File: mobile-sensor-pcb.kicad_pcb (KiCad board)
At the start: 2 copper layers, 101.6 x 53.3 mm, 93 parts, among them J1 SMA, J2 USB_OTG, J3 JST PH, Q1 PNP-BJT-BIASED_SOT, SW1 RESET, SW2 ON/OFF, U1 3M_2908-05WB-MG, U10 LP2980AIM5-3.3/NOPB, U11 LP2980AIM5-3.3/NOPB, U12 LP2980AIM5-3.3/NOPB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

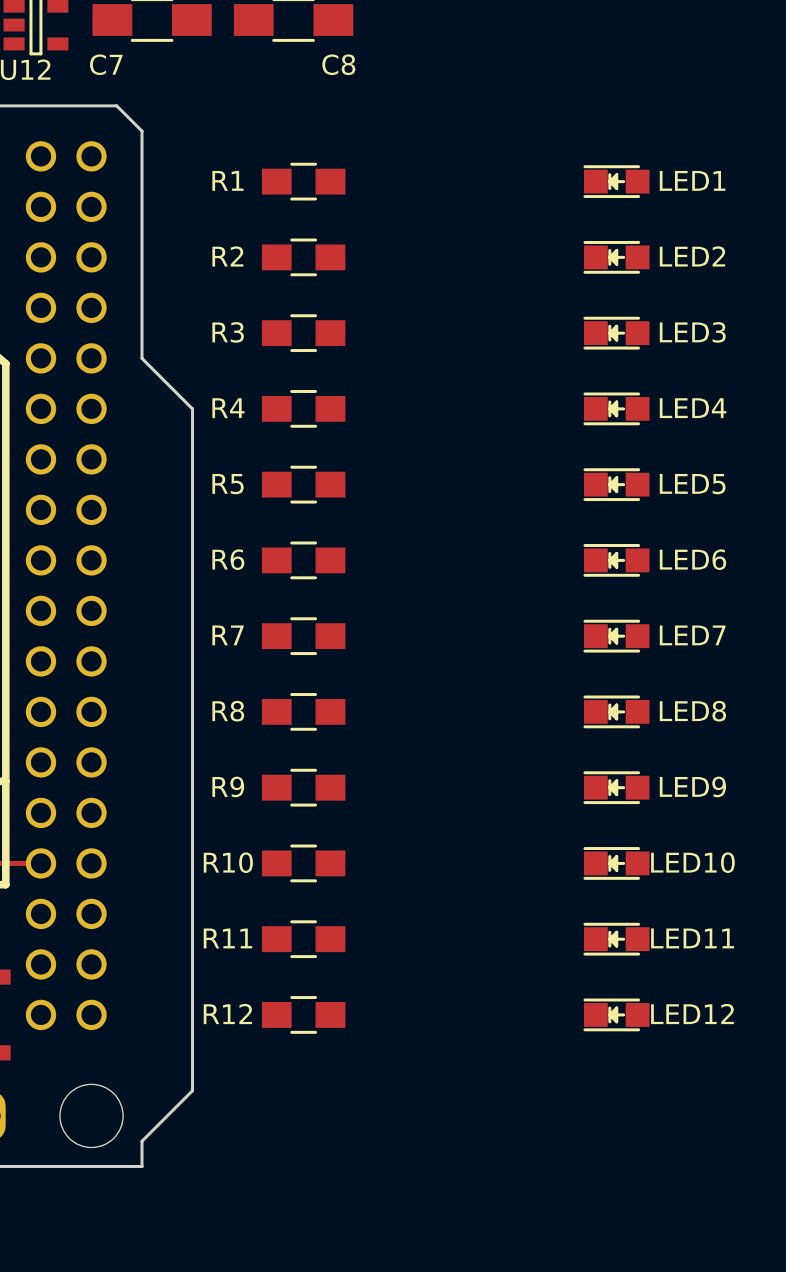
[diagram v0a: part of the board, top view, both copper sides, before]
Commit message: Tweak LED layout a little
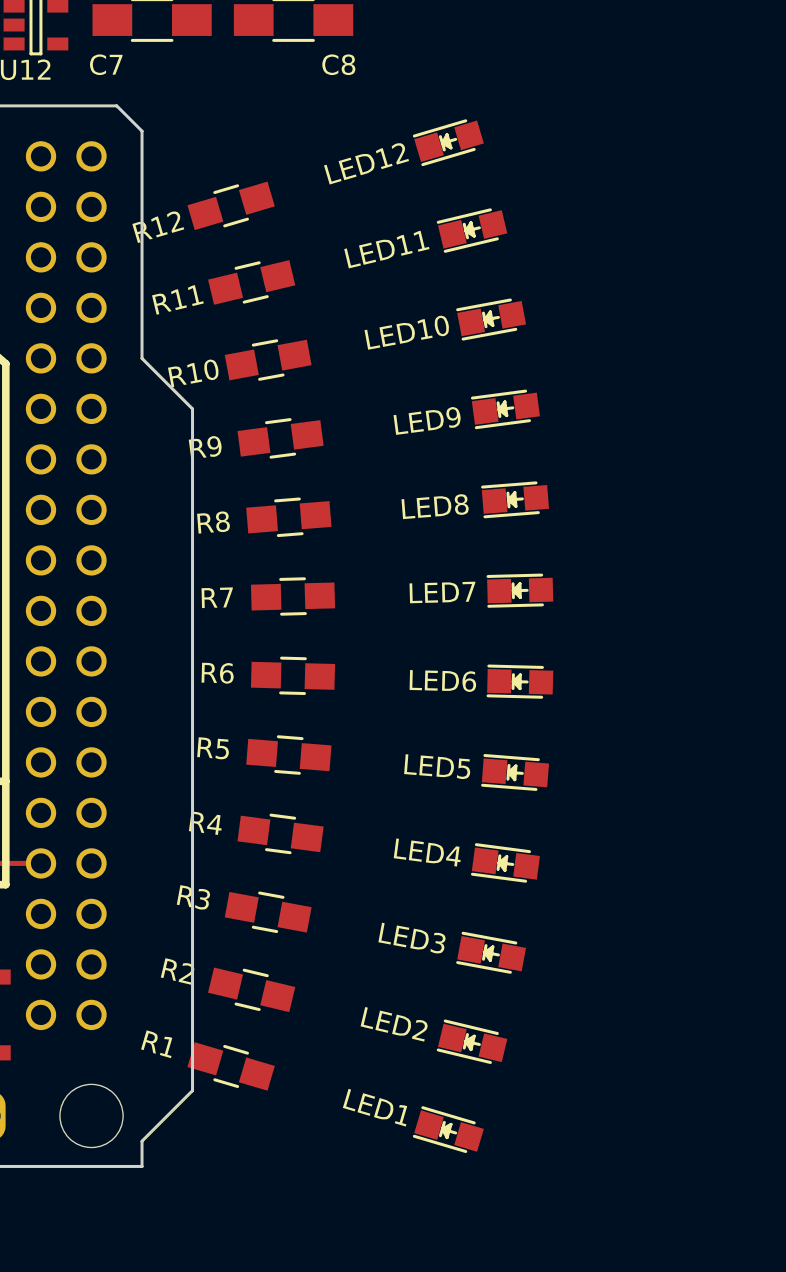
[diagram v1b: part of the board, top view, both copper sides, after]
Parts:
- moved LED1 48.5 mm to (165.3, 150.6), turned to 343.5 degrees
- moved LED12 44.7 mm to (165.3, 100.8), turned to 16.5 degrees
- moved R1 44.7 mm to (154.3, 147.4), turned to 343.5 degrees
- moved R12 40.9 mm to (154.3, 104.1), turned to 16.5 degrees
- moved LED2 40.2 mm to (166.5, 146.2), turned to 346.5 degrees
- moved R2 36.9 mm to (155.4, 143.5), turned to 346.5 degrees
- moved LED11 36.4 mm to (166.5, 105.3), turned to 13.5 degrees
- moved R11 33.1 mm to (155.4, 107.9), turned to 13.5 degrees
- moved LED3 31.8 mm to (167.4, 141.7), turned to 349.5 degrees
- moved R3 29.2 mm to (156.2, 139.6), turned to 349.5 degrees
- moved LED10 28.1 mm to (167.4, 109.8), turned to 10.5 degrees
- moved R10 25.4 mm to (156.2, 111.8), turned to 10.5 degrees
- moved LED4 23.5 mm to (168.2, 137.2), turned to 352.5 degrees
- moved R4 21.4 mm to (156.8, 135.7), turned to 352.5 degrees
- moved LED9 19.9 mm to (168.2, 114.3), turned to 7.5 degrees
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
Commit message: More routing
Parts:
- moved Q1 16.1 mm to (119.8, 106.2)
- moved C21 12.9 mm to (103.8, 115.1), turned to 270 degrees
- moved D1 6.84 mm to (112.9, 106.2), turned to 270 degrees
- moved F1 5.88 mm to (111.6, 112.5), turned to 270 degrees
- moved C20 5.59 mm to (106.4, 115.1), turned to 270 degrees
- turned R1 to 163.5 degrees
- turned R10 to 190.5 degrees
- turned R11 to 193.5 degrees
- turned R12 to 196.5 degrees
- turned R2 to 166.5 degrees
- turned R3 to 169.5 degrees
- turned R4 to 172.5 degrees
- turned R5 to 175.5 degrees
- turned R6 to 178.5 degrees
- turned R7 to 181.5 degrees
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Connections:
- C1 pad 1: Net-(C1-Pad1) -> BATT-5V
- C2 pad 1: Net-(C2-Pad1) -> XBEE-3V3
- R23 pad 1: Net-(R23-Pad1) -> Net-(C20-Pad1)
- R24 pad 1: Net-(R24-Pad1) -> Net-(C11-Pad1)
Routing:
- net GND: track 295.3 -> 460.8 mm, vias 6 -> 13
- net BATT-5V: track 9.49 -> 87.9 mm, vias 2 -> 5
- net SD-SCK: track 0.00 -> 77.1 mm, vias 0 -> 2
- net SD-MOSI: track 0.00 -> 71.7 mm, vias 0 -> 3
- net SD-CS: track 5.92 -> 77.0 mm, vias 0 -> 2
- net XBEE-RESET: track 0.00 -> 67.2 mm, vias 0 -> 2
- net XBEE-3V3: track 0.00 -> 67.0 mm, vias 0 -> 5
- net XBEE-RX: track 0.00 -> 51.3 mm, vias 0 -> 1
- net XBEE-TX: track 0.00 -> 50.9 mm, vias 0 -> 2
- net Net-(C20-Pad1): track 9.14 -> 52.3 mm, vias 0 -> 2
- net XBEE-DIO5: track 0.00 -> 32.9 mm, vias 0 -> 1
- net TC-SCK: track 0.00 -> 28.8 mm
- net Net-(C15-Pad2): track 0.00 -> 25.7 mm, vias 0 -> 1
- net TC-MISO: track 0.00 -> 24.9 mm
- net Net-(BT1-Pad1): track 0.00 -> 23.1 mm, vias 0 -> 1
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
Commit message: Route all but thermocouples. Add LED arc screenshots.
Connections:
- SHIELD1 pad 50: SD-SCK -> SD-CLK
- U2 pad 3: SD-SCK -> SD-CLK
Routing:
- net BATT-STAT: track 1.69 -> 137.2 mm, vias 1 -> 5
- net SD-CLK: track 1.59 -> 131.3 mm, vias 1 -> 4
- net GPS-FIX: track 1.63 -> 126.6 mm, vias 1 -> 4
- net USB-5V: track 13.5 -> 137.9 mm, vias 1 -> 4
- net GND: track 460.8 -> 558.5 mm
- net GPS-SD-3V3: track 75.7 -> 169.3 mm, vias 3 -> 6
- net BATT-5V: track 87.9 -> 172.6 mm, vias 5 -> 9
- net SD-SCK: track 77.1 -> 0.00 mm, vias 2 -> 0
- net XBEE-RSSI: track 1.59 -> 69.4 mm
- net GPS-TX: track 0.00 -> 61.9 mm, vias 0 -> 2
- net BATT-DEAD: track 1.56 -> 57.4 mm, vias 1 -> 2
- net TC-CS2: track 0.00 -> 47.9 mm, vias 0 -> 1
- net XBEE-3V3: track 67.0 -> 113.0 mm, vias 5 -> 6
- net GPS-5V-RX: track 20.3 -> 55.0 mm, vias 0 -> 2
- net Net-(Q1-Pad1): track 0.00 -> 26.3 mm, vias 0 -> 2
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
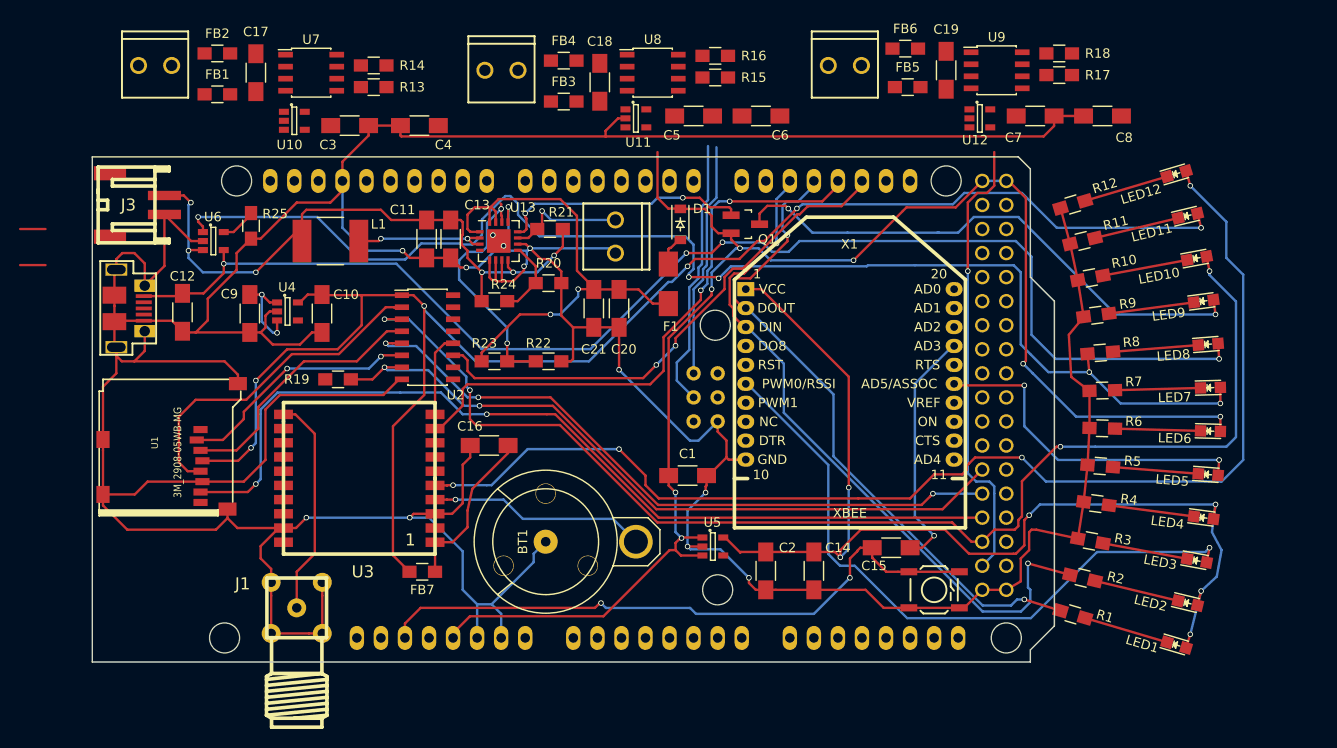
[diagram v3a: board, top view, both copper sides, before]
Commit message: Minor PCB fixes. Rework BOM to have fewer distributors. Change battery holder part.
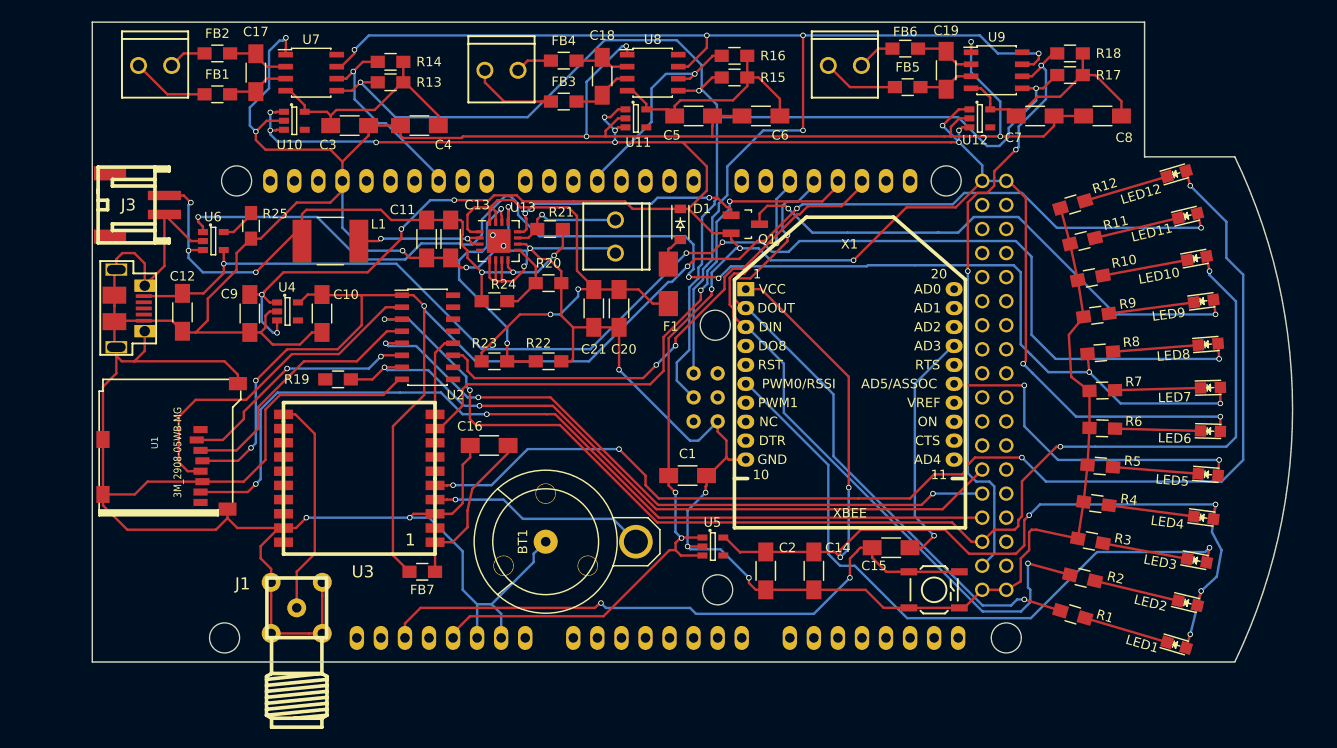
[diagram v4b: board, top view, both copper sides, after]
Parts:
- moved R15 2.03 mm to (118.6, 90.7)
- moved R16 2.03 mm to (118.6, 88.4)
- moved R13 1.85 mm to (82.3, 91.2)
- moved R14 1.82 mm to (82.3, 89.0)
- moved R17 1.14 mm to (154.1, 90.4)
- moved R18 1.14 mm to (154.1, 88.1)
- moved C18 0.68 mm to (104.6, 90.6)
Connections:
- R13 pad 1: Net-(R13-Pad1) -> Net-(C3-Pad1)
- R15 pad 1: Net-(R15-Pad1) -> Net-(C5-Pad1)
- R17 pad 1: Net-(R17-Pad1) -> Net-(C7-Pad1)
- U12 pad 1: Net-(U12-Pad1) -> BATT-5V
- U12 pad 3: Net-(U12-Pad1) -> BATT-5V
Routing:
- net BATT-5V: track 172.6 -> 322.0 mm, vias 9 -> 20
- net TC-SCK: track 28.6 -> 133.8 mm, vias 0 -> 3
- net TC-MISO: track 24.9 -> 127.2 mm, vias 0 -> 5
- net GND: track 558.5 -> 620.3 mm, vias 13 -> 19
- net Net-(C5-Pad1): track 0.00 -> 25.4 mm
- net Net-(C3-Pad1): track 0.00 -> 24.8 mm
- net Net-(C7-Pad1): track 0.00 -> 24.6 mm
- net TC-CS1: track 0.00 -> 23.0 mm, vias 0 -> 1
- net TC-CS0: track 0.00 -> 20.8 mm, vias 0 -> 1
- net TC-CS2: track 47.9 -> 64.4 mm, vias 1 -> 3
- net Net-(FB3-Pad1): track 0.00 -> 9.09 mm
- net Net-(FB1-Pad1): track 0.00 -> 8.24 mm
- net Net-(FB5-Pad1): track 0.00 -> 7.98 mm
- net Net-(C17-Pad1): track 0.00 -> 6.66 mm
- net Net-(C17-Pad2): track 0.00 -> 6.55 mm
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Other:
- board size 101.6 x 53.3 mm -> 126.8 x 67.6 mm
